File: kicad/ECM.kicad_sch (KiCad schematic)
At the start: 7 parts, among them J1 Bus_PCI_Express_x1, J6 USB_C_Receptacle_USB2.0_16P, U1 MCP25625T-E/ML, U2 RP2040, U4 W25Q128JVP, X1 ABM8-272-T3, Y1 X322516MLB4SI

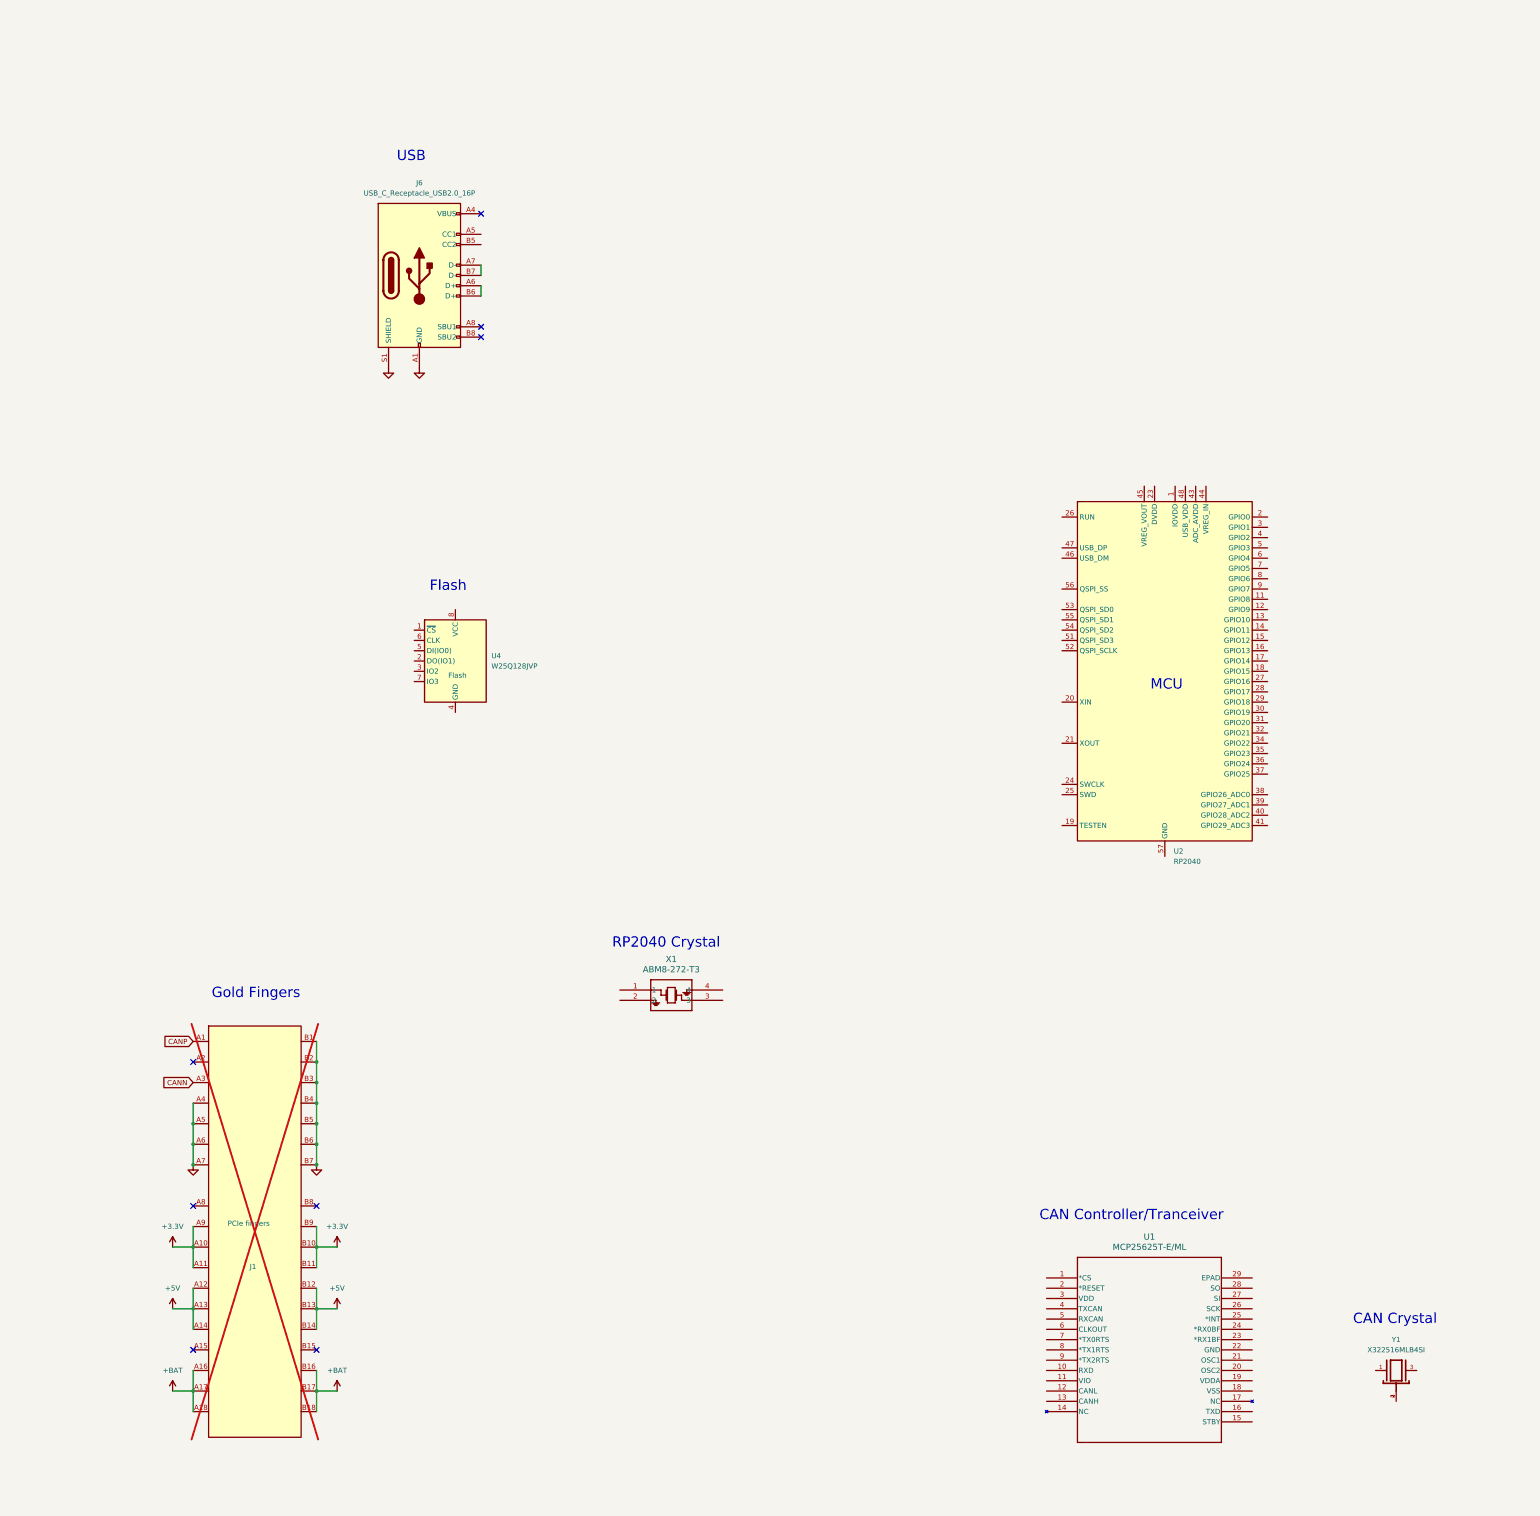
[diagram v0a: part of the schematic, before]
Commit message: Schematic Capture of RP2040, CAN Network, USB-C, Memory, DAQ, Servo Drivers and PWM Level Shifter.
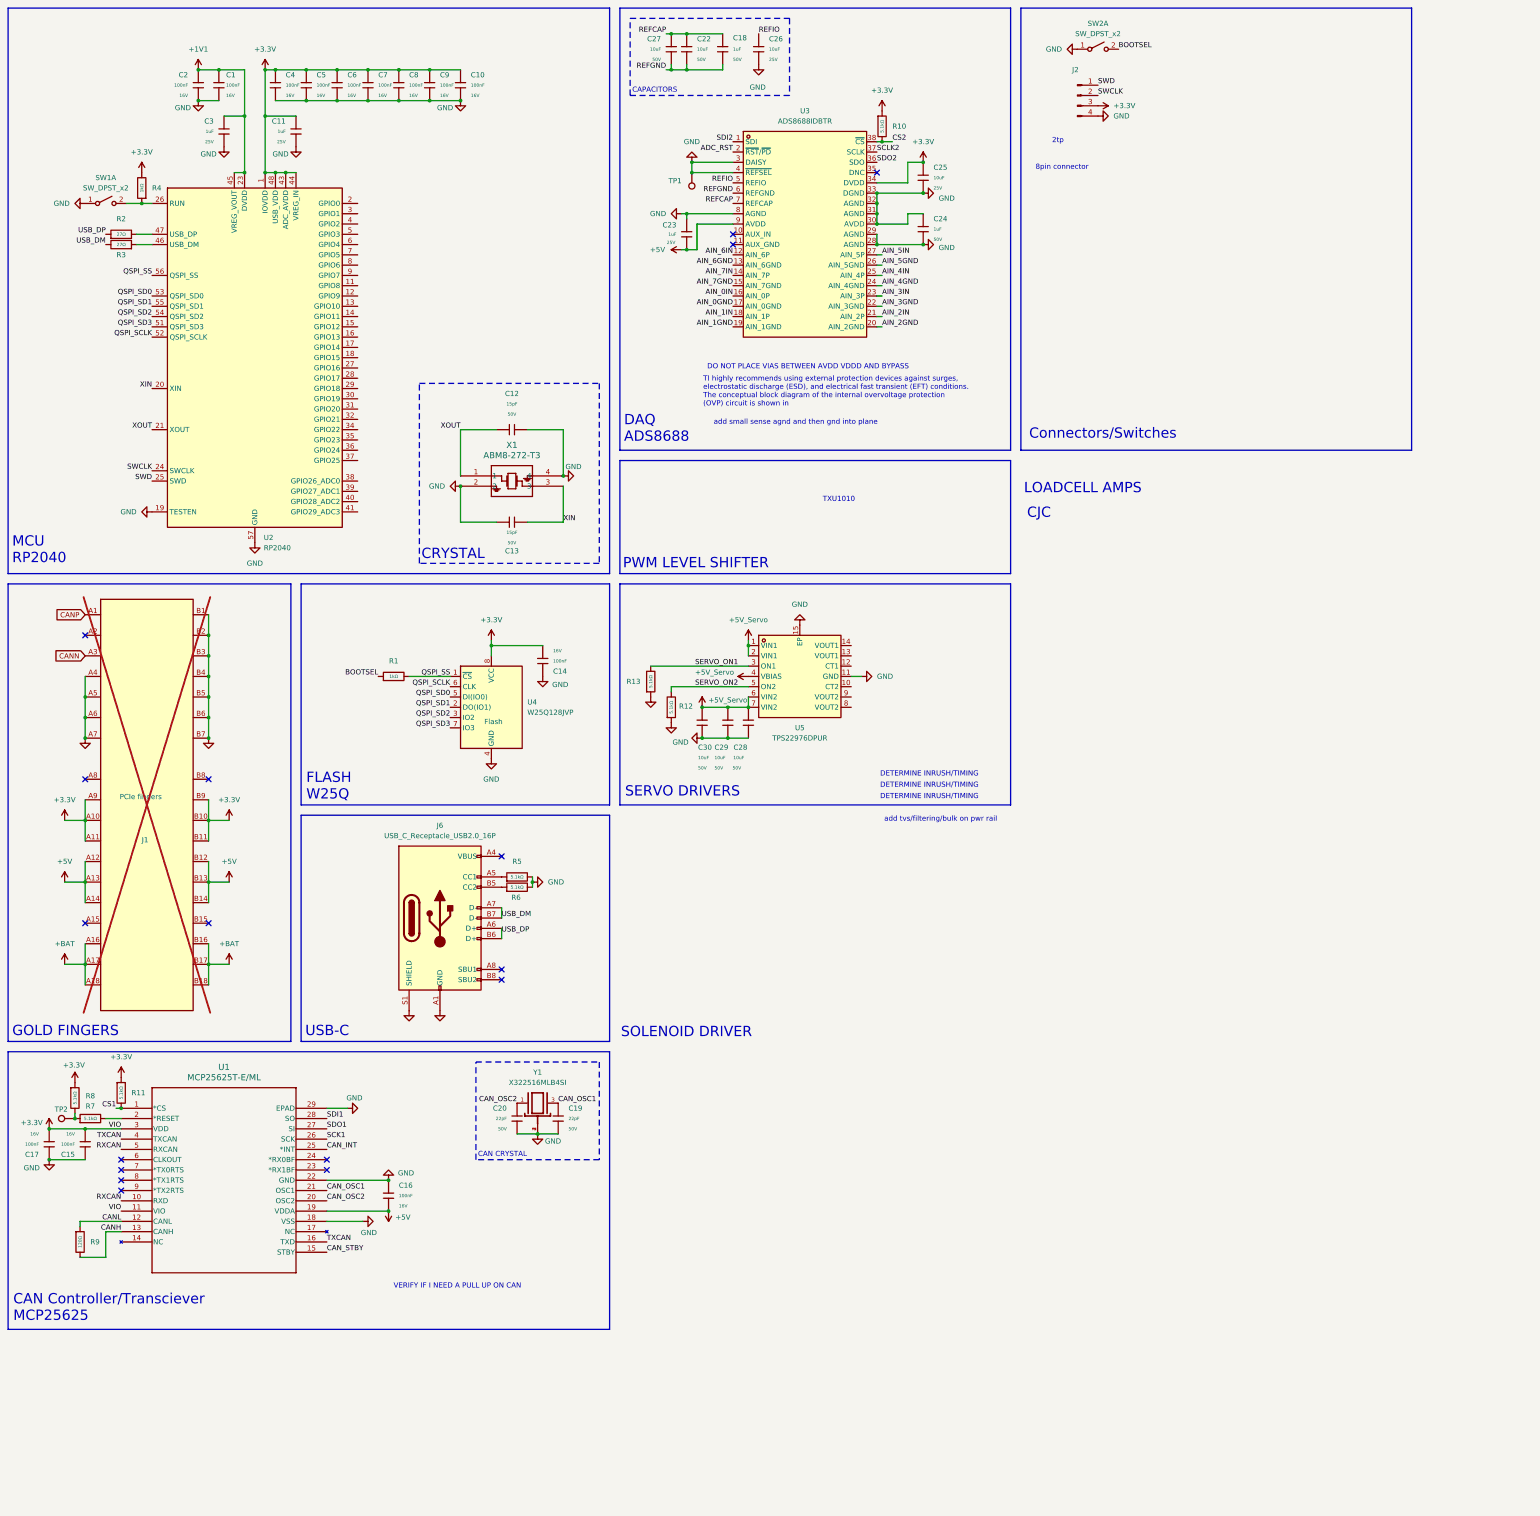
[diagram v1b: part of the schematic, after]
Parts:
- added C1, C10, C14, C15, C16, C17, C2, C4, C5, C6, C7, C8, C9: 100nF, PCM_JLCPCB:C_0402, symbol PCM_JLCPCB-Capacitors:0402,100nF
- added C11, C23, C3: 1uF, PCM_JLCPCB:C_0402, symbol PCM_JLCPCB-Capacitors:0402,1uF
- added C12, C13: 15pF, PCM_JLCPCB:C_0603, symbol PCM_JLCPCB-Capacitors:0603,15pF
- added C18, C24: 1uF, PCM_JLCPCB:C_0603, symbol PCM_JLCPCB-Capacitors:0603,1uF
- added C19, C20: 22pF, PCM_JLCPCB:C_0603, symbol PCM_JLCPCB-Capacitors:0603,22pF
- added C22, C27, C28, C29, C30: 10uF, PCM_JLCPCB:C_0805, symbol PCM_JLCPCB-Capacitors:0805,10uF,(2)
- added C25, C26: 10uF, PCM_JLCPCB:C_0805, symbol PCM_JLCPCB-Capacitors:0805,10uF
- added J2: Conn_01x04_Pin, symbol Connector:Conn_01x04_Pin
- added R1, R4: 1kΩ, PCM_JLCPCB:R_0603, symbol PCM_JLCPCB-Resistors:0603,1kΩ
- added R10, R11, R12, R13, R5, R6, R7, R8: 5.1kΩ, PCM_JLCPCB:R_0603, symbol PCM_JLCPCB-Resistors:0603,5.1kΩ
- added R2, R3: 27Ω, PCM_JLCPCB:R_0603, symbol PCM_JLCPCB-Resistors:0603,27Ω
- added R9: 120Ω, PCM_JLCPCB:R_0603, symbol PCM_JLCPCB-Resistors:0603,120Ω
- added SW1, SW2: SW_DPST_x2, symbol Switch:SW_DPST_x2
- added TP1, TP2: TestPoint, symbol Connector:TestPoint
- added U3: ADS8688IDBTR, easyeda2kicad:TSSOP-38_L9.7-W4.4-P0.50-LS6.4-BL, symbol easyeda2kicad:ADS8688IDBTR
- added U5: TPS22976DPUR, easyeda2kicad:WSON-14_L3.0-W2.0-P0.40-BL-EP-1, symbol easyeda2kicad:TPS22976DPUR
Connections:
- net +3.3V: now also U1.11 (VIO), U1.3 (VDD), U2.1 (IOVDD), U2.10 (IOVDD), U2.22 (IOVDD), U2.33 (IOVDD), U2.42 (IOVDD), U2.43 (ADC_AVDD), U2.44 (VREG_IN), U2.48 (USB_VDD), U2.49 (IOVDD), U4.8 (VCC), C10.1, C11.1, C14.2, C15.2, C17.2, C25.1, C4.1, C5.1, C6.1, C7.1, C8.1, C9.1, J2.3 (Pin_3), R10.1, R11.1, R4.2, R8.1, U3.34 (DVDD)
- net +5V: now also U1.19 (VDDA), C16.1, C23.2, U3.9 (AVDD)
- net GND: now also U1.18 (VSS), U1.22 (GND), U1.29 (EPAD), U2.19 (TESTEN), U2.57 (GND), U4.4 (GND), X1.2, X1.4, Y1.2, Y1.4, C1.2, C10.2, C11.2, C12.2, C13.2, C14.1, C15.1, C16.2, C17.1, C19.2, C2.2, C20.2, C23.1, C24.1, C24.2, C25.2, C26.1, C28.1, C29.2, C3.2, C30.2, C4.2, C5.2, C6.2, C7.2, C8.2, C9.2, J2.4 (Pin_4), R12.1, R13.1, R5.2, R6.2, SW1.1 (A), SW2.1 (A), TP1.1, U3.28 (AGND), U3.29 (AGND), U3.3 (DAISY), U3.30 (AVDD), U3.31 (AGND), U3.32 (AGND), U3.33 (DGND), U3.4 (~{REFSEL}), U3.8 (AGND), U5.11 (GND), U5.15 (EP)
- net CS1: now reaches U1.1 (*CS)
- net CS1: now also R11.2
- net RXCAN: now reaches U1.10 (RXD)
- net RXCAN: now also U1.5 (RXCAN)
- net CANL: now reaches U1.12 (CANL)
- net CANL: now also R9.1
- net CANH: now reaches U1.13 (CANH)
- net CANH: now also R9.2
- net CAN_STBY: now reaches U1.15 (STBY)
- net TXCAN: now reaches U1.16 (TXD)
- net TXCAN: now also U1.4 (TXCAN)
- net at U1.2 (*RESET): now also R7.2
- net CAN_OSC2: now reaches U1.20 (OSC2)
- net CAN_OSC2: now also Y1.1, C20.1
- net CAN_OSC1: now reaches U1.21 (OSC1)
- net CAN_OSC1: now also Y1.3, C19.1
- net CAN_INT: now reaches U1.25 (*INT)
- net SCK1: now reaches U1.26 (SCK)
- net SDO1: now reaches U1.27 (SI)
- net SDI1: now reaches U1.28 (SO)
- net QSPI_SS: now reaches U4.1 (~{CS})
- net QSPI_SS: now also U2.56 (QSPI_SS), R1.2
- net QSPI_SD1: now reaches U4.2 (DO(IO1))
- net QSPI_SD1: now also U2.55 (QSPI_SD1)
- net QSPI_SD2: now reaches U4.3 (IO2)
- net QSPI_SD2: now also U2.54 (QSPI_SD2)
- net QSPI_SD0: now reaches U4.5 (DI(IO0))
- net QSPI_SD0: now also U2.53 (QSPI_SD0)
- net QSPI_SCLK: now reaches U4.6 (CLK)
- net QSPI_SCLK: now also U2.52 (QSPI_SCLK)
- net QSPI_SD3: now reaches U4.7 (IO3)
- net QSPI_SD3: now also U2.51 (QSPI_SD3)
- net XIN: now reaches U2.20 (XIN)
- net XIN: now also X1.3, C13.1
- net XOUT: now reaches U2.21 (XOUT)
- net XOUT: now also X1.1, C12.1
- net +1V1: now reaches U2.23 (DVDD), U2.50 (DVDD)
- net +1V1: now also U2.45 (VREG_VOUT), C1.1, C2.1, C3.1
- net SWCLK: now reaches U2.24 (SWCLK)
- net SWCLK: now also J2.2 (Pin_2)
- net SWD: now reaches U2.25 (SWD)
- net SWD: now also J2.1 (Pin_1)
- net at U2.26 (RUN): now also R4.1, SW1.2 (B)
- net at U2.46 (USB_DM): now also R3.1
- net at U2.47 (USB_DP): now also R2.2
- net at J6.A5 (CC1): now also R5.1
- net USB_DP: now reaches J6.A6 (D+), J6.B6 (D+)
- net USB_DP: now also R2.1
- net USB_DM: now reaches J6.A7 (D-), J6.B7 (D-)
- net USB_DM: now also R3.2
- net at J6.B5 (CC2): now also R6.1
- new net: R7.1, R8.2, TP2.1
- new net +5V_Servo: C28.2, C29.1, C30.1, U5.1 (VIN1), U5.2 (VIN1), U5.4 (VBIAS), U5.6 (VIN2), U5.7 (VIN2)
- new net ADC_RST: U3.2 (~{RST}/~{PD})
- new net AIN_0GND: U3.17 (AIN_0GND)
- new net AIN_0IN: U3.16 (AIN_0P)
- new net AIN_1GND: U3.19 (AIN_1GND)
- new net AIN_1IN: U3.18 (AIN_1P)
- new net AIN_2GND: U3.20 (AIN_2GND)
- new net AIN_2IN: U3.21 (AIN_2P)
- new net AIN_3GND: U3.22 (AIN_3GND)
- new net AIN_3IN: U3.23 (AIN_3P)
- new net AIN_4GND: U3.24 (AIN_4GND)
- new net AIN_4IN: U3.25 (AIN_4P)
- new net AIN_5GND: U3.26 (AIN_5GND)
- new net AIN_5IN: U3.27 (AIN_5P)
- new net AIN_6GND: U3.13 (AIN_6GND)
- new net AIN_6IN: U3.12 (AIN_6P)
- new net AIN_7GND: U3.15 (AIN_7GND)
- new net AIN_7IN: U3.14 (AIN_7P)
- new net BOOTSEL: R1.1, SW2.2 (B)
- new net CS2: R10.2, U3.38 (~{CS})
- new net REFCAP: C18.1, C22.1, C27.2, U3.7 (REFCAP)
- new net REFGND: C18.2, C22.2, C27.1, U3.6 (REFGND)
- new net REFIO: C26.2, U3.5 (REFIO)
- new net SCLK2: U3.37 (SCLK)
- new net SDI2: U3.1 (SDI)
- new net SDO2: U3.36 (SDO)
- new net SERVO_ON1: R13.2, U5.3 (ON1)
- new net SERVO_ON2: R12.2, U5.5 (ON2)
- no-connect marks 8 -> 17
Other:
- note added: "2tp"
- note added: "8pin connector"
- note added: "CAN CRYSTAL"
- note added: "CAN Controller/Transciever MCP25625"
- note added: "CAPACITORS"
- note added: "CJC"
- note added: "CRYSTAL"
- note added: "Connectors/Switches"
- note added: "DAQ ADS8688"
- note added: "DETERMINE INRUSH/TIMING"
- note added: "DO NOT PLACE VIAS BETWEEN AVDD VDDD AND BYPASS"
- note added: "FLASH W25Q"
- note added: "GOLD FINGERS"
- note added: "LOADCELL AMPS"
- note added: "MCU RP2040"
- note added: "PWM LEVEL SHIFTER"
- note added: "SERVO DRIVERS"
- note added: "SOLENOID DRIVER"
- note added: "TI highly recommends using external protection devices against surges, electrostatic discharge (ESD), and electrical fast transient (EFT) conditions. The conceptual block diagram of the internal overvoltage protection (OVP) circuit is shown in"
- note added: "TXU1010"
- note added: "USB-C"
- note added: "VERIFY IF I NEED A PULL UP ON CAN"
- note added: "add small sense agnd and then gnd into plane"
- note added: "add tvs/filtering/bulk on pwr rail"
- note removed: "CAN Controller/Tranceiver"
- note removed: "CAN Crystal"
- note removed: "Flash"
- note removed: "Gold Fingers"
- note removed: "MCU"
- note removed: "RP2040 Crystal"
- note removed: "USB"
- moved on the sheet: J1, J6, U1, U2, U4, X1, Y1

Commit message: Added control circuitry for Servos, PWM Level Shifting, and Solenoid Driving, Next Steps: Thermocouples and CJC
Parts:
- removed C28, C29, C30: 10uF, PCM_JLCPCB:C_0805, symbol PCM_JLCPCB-Capacitors:0805,10uF,(2)
- removed R7, R8: 5.1kΩ, PCM_JLCPCB:R_0603, symbol PCM_JLCPCB-Resistors:0603,5.1kΩ
- added C21, C28: 1uF, PCM_JLCPCB:C_0603, symbol PCM_JLCPCB-Capacitors:0603,1uF
- added C29, C30: 100nF, PCM_JLCPCB:C_0402, symbol PCM_JLCPCB-Capacitors:0402,100nF
- added C31: 22nF, PCM_JLCPCB:C_0603, symbol PCM_JLCPCB-Capacitors:0603,22nF
- added D1: SS210, PCM_JLCPCB:D_SMA, symbol PCM_JLCPCB-Diodes:Schottky,SS210
- added Q1, Q2: AO3400A, PCM_JLCPCB:Q_SOT-23, symbol PCM_JLCPCB-Transistors:NMOS,AO3400A
- added R14, R21: 10Ω, PCM_JLCPCB:R_0603, symbol PCM_JLCPCB-Resistors:0603,10Ω
- added R15, R18: 120Ω, PCM_JLCPCB:R_0603, symbol PCM_JLCPCB-Resistors:0603,120Ω
- added R16, R17, R19, R20: 5.1kΩ, PCM_JLCPCB:R_0603, symbol PCM_JLCPCB-Resistors:0603,5.1kΩ
- added R22, R23, R24: 10kΩ, PCM_JLCPCB:R_0402, symbol PCM_JLCPCB-Resistors:0402,10kΩ
- added R7: 300Ω, PCM_JLCPCB:R_0603, symbol PCM_JLCPCB-Resistors:0603,300Ω
- added R8: 27Ω, PCM_JLCPCB:R_0603, symbol PCM_JLCPCB-Resistors:0603,27Ω
- added U6: GAQY252G3S, easyeda2kicad:SOP-4_L4.3-W4.4-P2.54-LS7.0-BL, symbol easyeda2kicad:GAQY252G3S
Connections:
- net +3.3V: now also R15.1, R16.2, R17.2, R18.1, R22.2, R23.2, R24.2, R7.1
- net +5V_Servo: now also C21.1, C28.1, R19.2, R20.2
- net GND: now also C21.2, C28.2, C29.2, C30.2, D1.1, R14.2, R16.1, R17.1, R21.2, R8.2, U6.2, U6.3
- net at U1.2 (*RESET): now also TP2.1, R24.1
- net SERVO_PWR1: now reaches U5.13 (VOUT1)
- net SERVO_PWR1: now also U5.14 (VOUT1), C29.1, R14.1
- net SERVO_PWR2: now reaches U5.8 (VOUT2)
- net SERVO_PWR2: now also U5.9 (VOUT2), C30.1, R21.1
- new net: Q1.1 (G), R15.2
- new net: C31.2, R8.1
- new net: R7.2, U6.1
- new net: Q2.1 (G), R18.2
- new net +24V: C31.1, D1.2, U6.4
- new net 3.3V_PWM1: Q1.2 (S), R22.1
- new net 3.3V_PWM2: Q2.2 (S), R23.1
- new net 5V_PWM1: Q1.3 (D), R20.1
- new net 5V_PWM2: Q2.3 (D), R19.1
- no-connect marks 17 -> 19
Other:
- note added: "4IN-ENGINE CONTROL MODULE"
- note added: "DETERMINE IF RL IS NEEDED"
- note added: "SERVO PWR SWITCH"
- note added: "are snubber,TVS necessary? if so calc rise/fall is"
- note added: "mayb add a pull up on da gate so the pin isnt sinking current"
- note added: "send sim files ova"
- note removed: "SERVO DRIVERS"
- note removed: "TXU1010"
- note removed: "VERIFY IF I NEED A PULL UP ON CAN"
- note removed: "challenge template 0.1.0"
- moved on the sheet: C14, J2, SW2A

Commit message: Added thermocouple ICs and dc/dc circuitry for servo power
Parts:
- added C32, C33, C34, C35, C37: 100nF, PCM_JLCPCB:C_0402, symbol PCM_JLCPCB-Capacitors:0402,100nF
- added C36: 2.2uF, PCM_JLCPCB:C_0805, symbol PCM_JLCPCB-Capacitors:0805,2.2uF
- added C38, C39: 10uF, PCM_JLCPCB:C_0805, symbol PCM_JLCPCB-Capacitors:0805,10uF,(2)
- added D2: White, PCM_JLCPCB:D_0603, symbol PCM_JLCPCB-Diodes:LED,0603,White
- added Q3: AO3400A, PCM_JLCPCB:Q_SOT-23, symbol PCM_JLCPCB-Transistors:NMOS,AO3400A
- added R25, R26, R27, R28, R32, R34: 5.1kΩ, PCM_JLCPCB:R_0603, symbol PCM_JLCPCB-Resistors:0603,5.1kΩ
- added R29: 10kΩ, PCM_JLCPCB:R_0402, symbol PCM_JLCPCB-Resistors:0402,10kΩ
- added R30: 160kΩ, PCM_JLCPCB:R_0603, symbol PCM_JLCPCB-Resistors:0603,160kΩ
- added R31: 22kΩ, PCM_JLCPCB:R_0603, symbol PCM_JLCPCB-Resistors:0603,22kΩ
- added R33, R35: 120Ω, PCM_JLCPCB:R_0603, symbol PCM_JLCPCB-Resistors:0603,120Ω
- added SW3: SW_DPDT_x2, symbol Switch:SW_DPDT_x2
- added U10, U7, U8, U9: MAX31855KASA+T, easyeda2kicad:SO-8_L4.9-W3.9-P1.27-LS5.9-BL, symbol easyeda2kicad:MAX31855KASA+T
- added U11: SY8388ARHC, easyeda2kicad:QFN-16_L2.5-W2.5-P0.45-TL-EP0.6, symbol easyeda2kicad:SY8388ARHC
- C31, R8: now not fitted
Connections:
- net +24V: now also C38.2, C39.1, SW3.1 (A), U11.2 (IN), U11.3 (IN), U11.4 (IN), U11.9 (EN)
- net +3.3V: now also R25.2, R26.2, R27.2, R28.2
- net +5V_Servo: now also R30.1, R33.1, R34.2
- net GND: now also C32.1, C33.1, C34.1, C35.1, C36.2, C38.1, C39.2, D2.1, R29.1, R31.2, SW3.3 (C), U10.1 (GND), U11.14 (GND), U11.17 (GND), U11.6 (GND), U7.1 (GND), U8.1 (GND), U9.1 (GND)
- net SDO2: now also U10.7 (SO), U7.7 (SO), U8.7 (SO), U9.7 (SO)
- new net: C35.2, U10.4 (VCC)
- new net: R32.1, SW3.2 (B)
- new net: C34.2, U9.4 (VCC)
- new net: C37.2, U11.1 (BS)
- new net: R29.2, U11.10 (ILMT)
- new net: C36.1, U11.13 (VCC)
- new net: Q3.1 (G), R34.1, U11.7 (PG)
- new net: R33.2, R35.1
- new net: Q3.3 (D), R35.2
- new net: C32.2, U7.4 (VCC)
- new net: D2.2, Q3.2 (S)
- new net: C33.2, U8.4 (VCC)
- new net CS3: R28.1, U10.6 (~{CS})
- new net CS4: R25.1, U7.6 (~{CS})
- new net CS5: R26.1, U8.6 (~{CS})
- new net CS6: R27.1, U9.6 (~{CS})
- new net FB: R30.2, R31.1, U11.11 (FB)
- new net LX: C37.1, U11.15 (LX), U11.16 (LX), U11.5 (LX)
- new net MODE: R32.2, U11.8 (MODE)
- new net SCK2: U10.5 (SCK), U7.5 (SCK), U8.5 (SCK), U9.5 (SCK)
- new net T_1+: U10.3 (T+)
- new net T_1-: U10.2 (T-)
- new net T_2+: U7.3 (T+)
- new net T_2-: U7.2 (T-)
- new net T_3+: U8.3 (T+)
- new net T_3-: U8.2 (T-)
- new net T_4+: U9.3 (T+)
- new net T_4-: U9.2 (T-)
- no-connect marks 19 -> 23
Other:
- note added: "CALC TRANSIETN OF INDUCTOR"
- note added: "DC/DC CONVERTER"
- note added: "THERMOCOUPLE ICS"
- note added: "doubl echeck buck it prolly works tho"
- note removed: "CJC"
- note removed: "Connectors/Switches"
- note removed: "LOADCELL AMPS"
